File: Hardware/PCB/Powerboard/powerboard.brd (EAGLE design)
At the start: 29 x 18 mm, 13 parts, among them IC1 TP4056

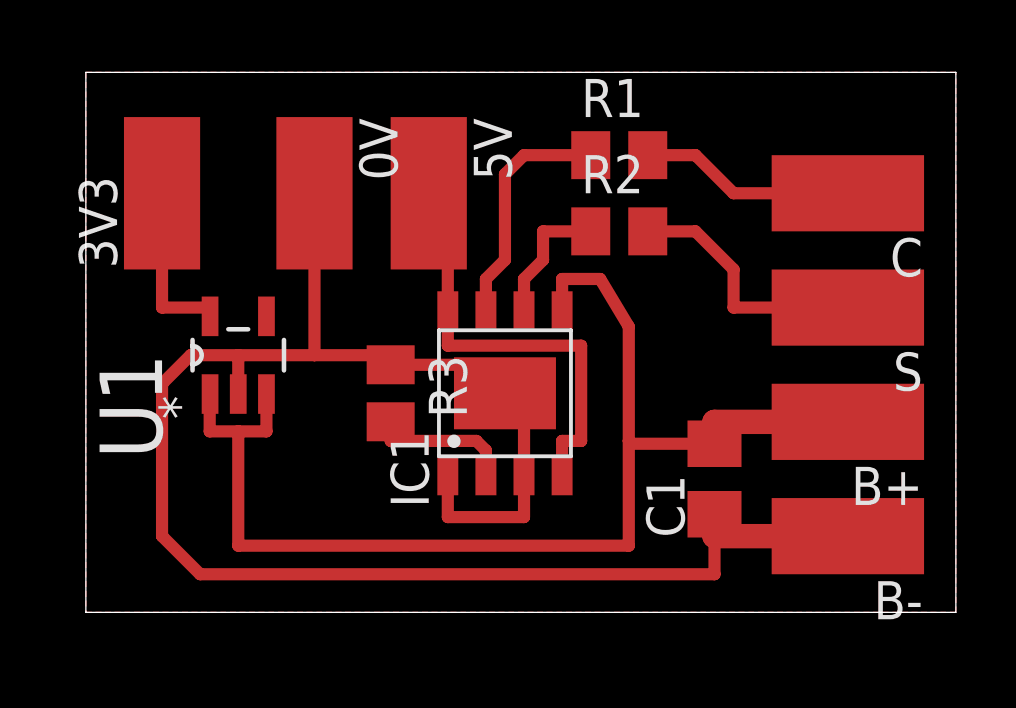
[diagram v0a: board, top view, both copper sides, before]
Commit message: cloud push
- PCB size & pattern modified
- Enclosure minor fix
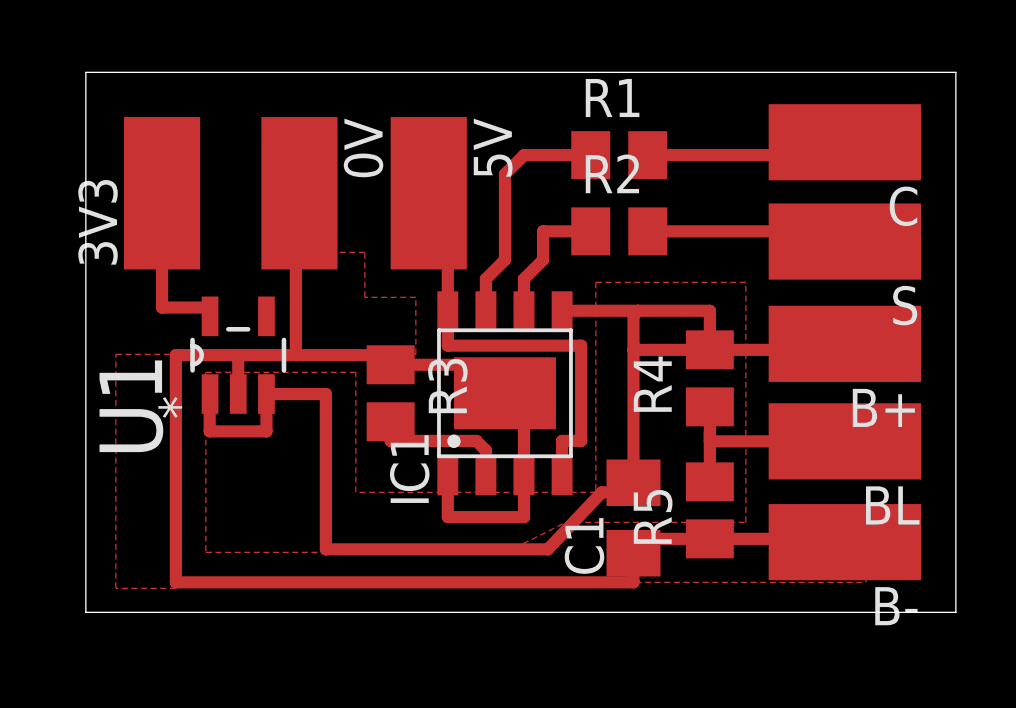
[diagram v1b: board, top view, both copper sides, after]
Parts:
- added BL: (no value), wirepad:SMD2,54-5,08
- added R4, R5: 103, rcl:M2012
- moved C1 3.00 mm to (18.3, 3.15)
- moved B+ 2.60 mm to (25.3, 8.95)
- moved S 2.20 mm to (25.3, 12.4)
- moved C 1.70 mm to (25.3, 15.7)
- moved 0V 0.50 mm to (7.12, 14.0)
- moved B- 0.22 mm to (25.3, 2.34)
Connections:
- new net BATLV: BL.1, R4.1, R5.2
- net BAT+: now also R4.2
- net GND: now also R5.1
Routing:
- net BATLV: track 0.00 -> 7.30 mm
- net P_ST: track 8.47 -> 6.91 mm
- net BAT+: track 40.8 -> 42.0 mm
- added copper zone on layer 1, net BAT+
